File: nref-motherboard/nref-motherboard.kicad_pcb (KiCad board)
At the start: 6 copper layers, 122.6 x 80 mm, 210 parts, among them J1 POWSW, J10 DISP, J11 BAT1, J12 BAT2, J13 SYSCTL_USB, J16 Conn_01x10_Pin, J17 Conn_01x10_Pin, J18 Conn_01x20, J19 SER, J2 Conn_01x12_Pin, J4 1-2199230-6, J5 SYSCTL, J6 USB_INT1, J7 PWR, J8 Conn_01x12_Pin, J9 Conn_01x14_Pin, Q1 NTMFD6H840NL, Q2 NTMFD6H840NL, SW2 RESET, SW4 SW_DIP_x08, U1 reform2-som-connector, U10 BQ25756RRVR, U11 LM62460, U2 74HC573, U3 MAX1837EUT33+T, U4 Si52111-B5, U5 LM62460, U7 USB2514B_Bi, U8 RP2040, U9 W25Q32JVSS, Y1 12MHz 18pF, Y2 24MHz, Y3 25MHz

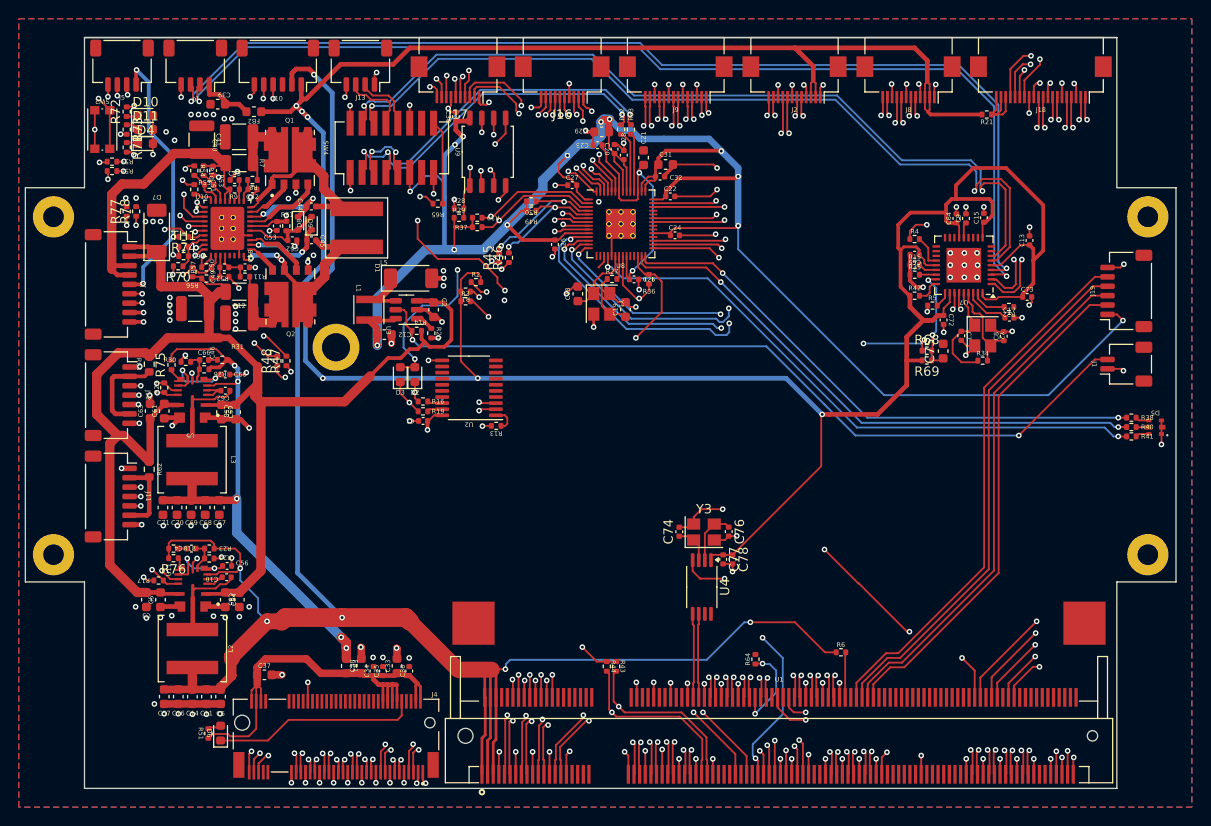
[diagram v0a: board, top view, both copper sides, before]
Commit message: mb silkscreen cleaned up
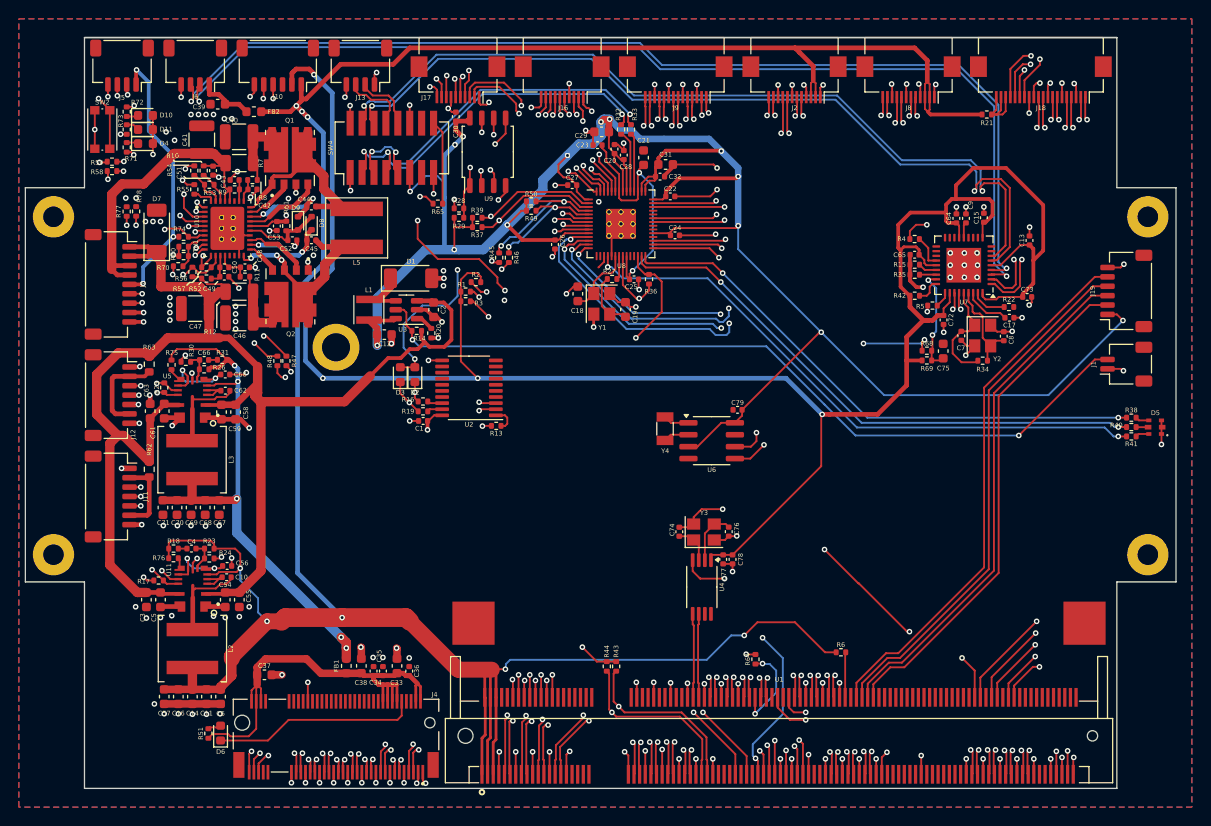
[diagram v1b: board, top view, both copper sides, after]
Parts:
- added C79: 0.1uF, Capacitor_SMD:C_0402_1005Metric, F.Cu at (99.6, 139.7)
- added U6: PCF8523T, Package_SO:SOIC-8_3.9x4.9mm_P1.27mm, F.Cu at (96.8, 143.0)
- added Y4: 32.768 kHz, Crystal:Crystal_SMD_3215-2Pin_3.2x1.5mm, F.Cu at (91.9, 141.7)
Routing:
- net STANDBY_3V3: track 337.0 -> 356.5 mm, vias 19 -> 20
- net DAC_SDA: track 105.7 -> 109.4 mm, vias 3 -> 4
- net DAC_SCL: track 108.7 -> 112.2 mm, vias 3 -> 4
- net Net-(U6-OSCI): track 0.00 -> 2.75 mm
- net Net-(U6-OSCO): track 0.00 -> 2.75 mm
- net GND: track 281.2 -> 282.2 mm, vias 203 -> 204

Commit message: mb fully routed, logo added
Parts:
- added G***: LOGO, footprints:nref-logo, F.Cu at (107.5, 138.3)

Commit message: motherboard d-1 production snapshot
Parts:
- added H7: BADGE, footprints:nref-motherboard-badge, F.Cu at (60.7, 147.5)
- added TP1: TestPoint, TestPoint:TestPoint_Pad_1.0x1.0mm, F.Cu at (121.7, 115.8)
- added TP2: TestPoint, TestPoint:TestPoint_Pad_1.0x1.0mm, F.Cu at (119.7, 115.8)
- added TP3: TestPoint, TestPoint:TestPoint_Pad_1.0x1.0mm, F.Cu at (142.4, 148.9)
- added TP4: TestPoint, TestPoint:TestPoint_Pad_1.0x1.0mm, F.Cu at (144.4, 148.9)
- H6: renamed from G***; footprint footprints:nref-logo -> footprints:nref-reflex-logo
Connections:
- U7 pad 8: unconnected-(U7-USBDM_DN4/PRT_DIS_M4-Pad8) -> USB2D_DN
- U7 pad 9: unconnected-(U7-USBDP_DN4/PRT_DIS_P4-Pad9) -> USB2D_DP
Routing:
- net HDMI_AUXN: track 0.00 -> 35.3 mm, vias 0 -> 2
- net HDMI_AUXP: track 0.00 -> 34.5 mm, vias 0 -> 2
- net USB2D_DN: track 0.00 -> 17.0 mm, vias 0 -> 2
- net USB2D_DP: track 0.00 -> 16.7 mm, vias 0 -> 2
- net RP_FUSB_INT: track 1.47 -> 7.54 mm, vias 0 -> 1
- net USB2C_DP: track 89.1 -> 90.1 mm
- net USB2C_DN: track 89.5 -> 90.5 mm
- net USB2B_DN: track 112.7 -> 113.3 mm
- net USB2B_DP: track 113.3 -> 113.8 mm
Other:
- board text added: "LOOKING LIKE AN ICON"
